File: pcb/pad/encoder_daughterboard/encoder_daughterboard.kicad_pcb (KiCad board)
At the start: 2 copper layers, 91.4 x 26.9 mm, 9 parts, among them J1 Conn_01x12, SW1 RotaryEncoder_Switch_MP, SW2 RotaryEncoder_Switch_MP, SW3 RotaryEncoder_Switch_MP

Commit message: Update encoder_daughterboard
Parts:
- D1, D2, D3: moved to B.Cu
- J1: value Conn_01x12 -> AFA07-S12FCA-00; moved to B.Cu
- SW1, SW2, SW3: value RotaryEncoder_Switch_MP -> EC11E09244BS
- moved H1 51.2 mm to (95.2, 78.2)
- moved H2 49.7 mm to (120.2, 78.2)
- moved D3 14.7 mm to (139.2, 72.2)
- moved D2 2.26 mm to (117.2, 72.2)
- moved D1 2.25 mm to (91.9, 72.2)
- moved J1 1.90 mm to (120.2, 88.2), turned to 180 degrees
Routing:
- net BRow0: track 54.1 -> 0.00 mm
- net E0A: track 48.4 -> 0.00 mm
- net E0B: track 41.6 -> 0.00 mm
- net BCol0: track 38.0 -> 0.00 mm, vias 1 -> 0
- net E1A: track 26.2 -> 0.00 mm
- net BCol2: track 23.2 -> 0.00 mm
- net E1B: track 20.3 -> 0.00 mm
- net E2A: track 14.1 -> 0.00 mm
- net Net-(D3-A): track 16.7 -> 3.56 mm
- net BCol1: track 11.7 -> 0.00 mm, vias 1 -> 0
- net E2B: track 11.3 -> 0.00 mm
- net Net-(D2-A): track 5.81 -> 0.00 mm
- net Net-(D1-A): track 5.81 -> 0.00 mm
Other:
- board size 91.4 x 26.9 mm -> 70 x 21 mm

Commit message: Update encoder_daughterboard
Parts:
- H1: value MountingHole_Pad_MP -> MountingHole_Pad
- moved H2 1.00 mm to (121.2, 78.2)
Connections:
- H1 pad 1: (no net) -> GND
- J1 pad 1: E0B -> BCol2
- J1 pad 10: BCol2 -> BCol0
- J1 pad 11: BRow0 -> E0A
- J1 pad 12: GND -> E0B
- J1 pad 2: E0A -> E2B
- J1 pad 3: E1B -> E2A
- J1 pad 4: E1A -> BRow0
- J1 pad 5: E2A -> E1A
- J1 pad 6: E2B -> E1B
- J1 pad 7: GND -> BCol1
- J1 pad 8: BCol0 -> GND
- J1 pad 9: BCol1 -> GND
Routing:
- net BRow0: track 0.00 -> 59.8 mm
- net E0A: track 0.00 -> 45.1 mm
- net E0B: track 0.00 -> 42.1 mm
- net BCol0: track 0.00 -> 29.5 mm
- net E1A: track 0.00 -> 25.1 mm
- net E1B: track 0.00 -> 23.7 mm
- net BCol2: track 0.00 -> 16.7 mm
- net E2A: track 0.00 -> 10.8 mm
- net BCol1: track 0.00 -> 6.71 mm
- net E2B: track 0.00 -> 4.74 mm
- net Net-(D2-A): track 0.00 -> 3.54 mm
- net Net-(D1-A): track 0.00 -> 3.50 mm
- net GND: track 0.00 -> 3.04 mm, vias 0 -> 4
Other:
- outline, holes or cut-outs redrawn

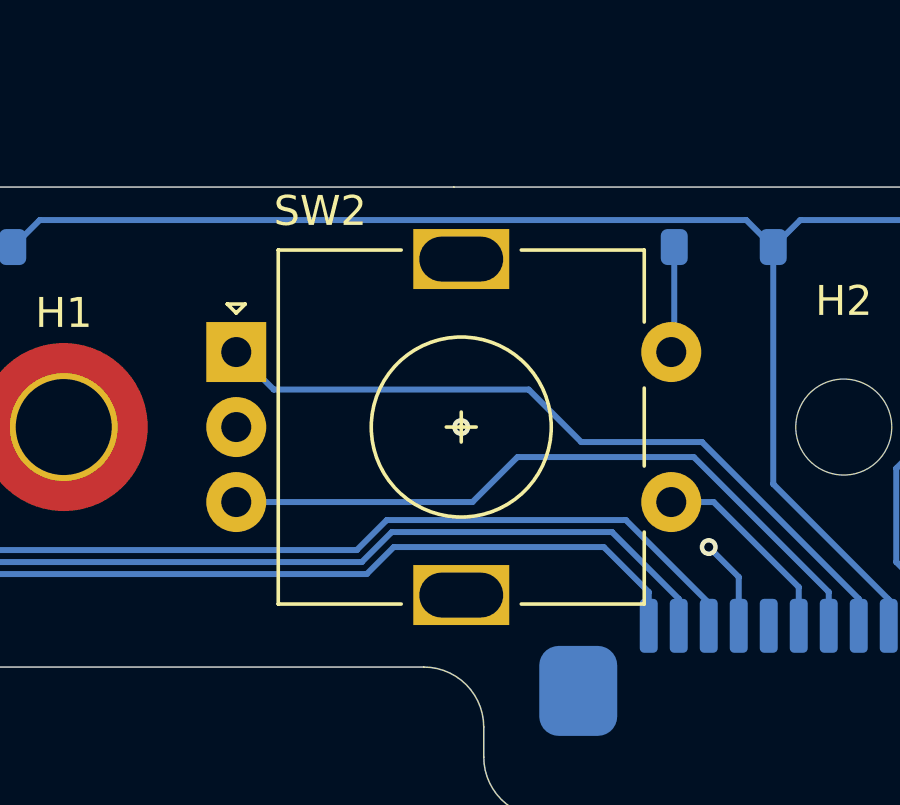
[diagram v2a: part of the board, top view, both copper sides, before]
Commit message: Fix center encoder position
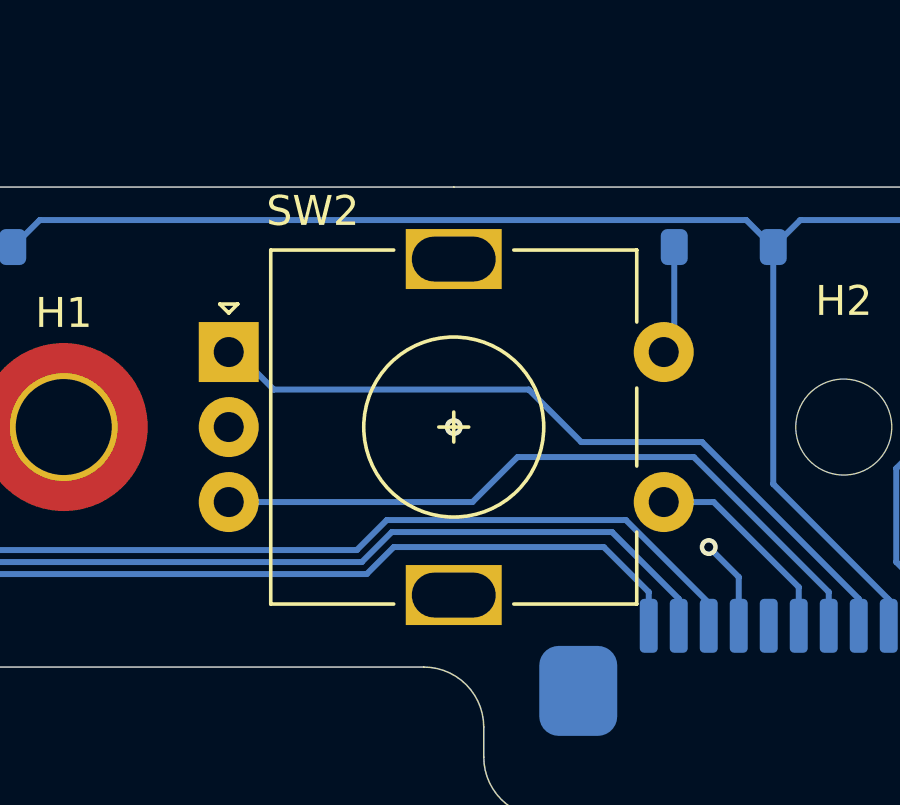
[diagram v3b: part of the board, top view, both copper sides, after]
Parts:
- moved SW2 0.25 mm to (100.7, 75.7)
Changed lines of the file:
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@@
 	(footprint "Rotary_Encoder:RotaryEncoder_Alps_EC11E-Switch_Vertical_H20mm"
 		(layer "F.Cu")
-		(at 100.98 75.735)
+		(at 100.73 75.735)
 		(descr "Alps rotary encoder, EC12E... with switch, vertical shaft, http://www.alps.com/prod/info/E/HTML/Encoder/Incremental/EC11/EC11E15204A3.html")
 		(tags "rotary encoder")
@@
 	)
 	(via
-		(at 108.48 78.235)
+		(at 108.23 78.235)
 		(size 0.6)
 		(drill 0.3)
